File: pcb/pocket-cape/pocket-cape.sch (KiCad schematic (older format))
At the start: 28 parts, among them J1 PhDiode1, J2 12V, J3 PhDiode2, U1 MIC920, U2 74LVC2G14GV, U3 ULN2003A, U4 AP3211, U5 MIC920

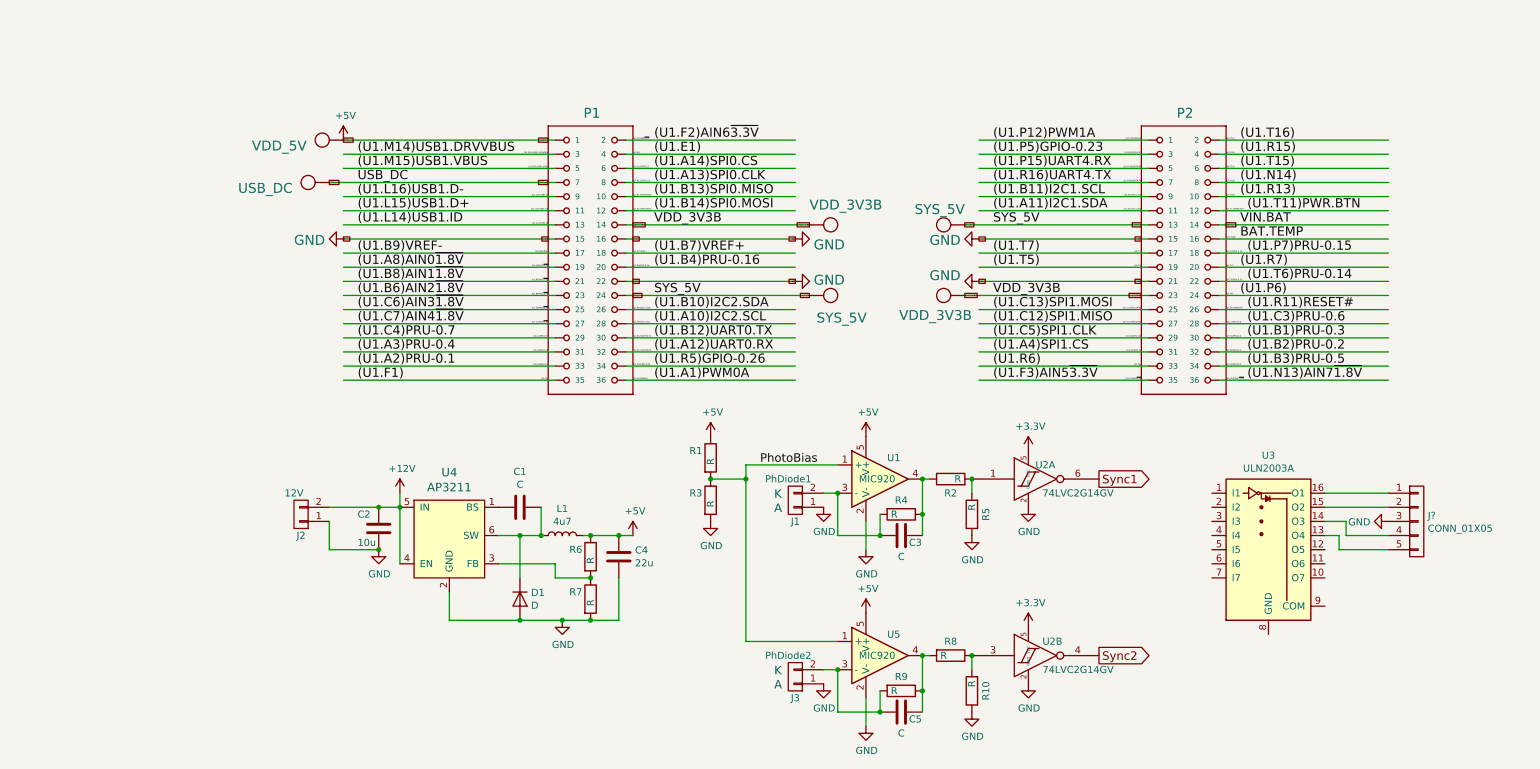
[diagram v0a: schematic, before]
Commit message: Pocket Cape, pre-routing.
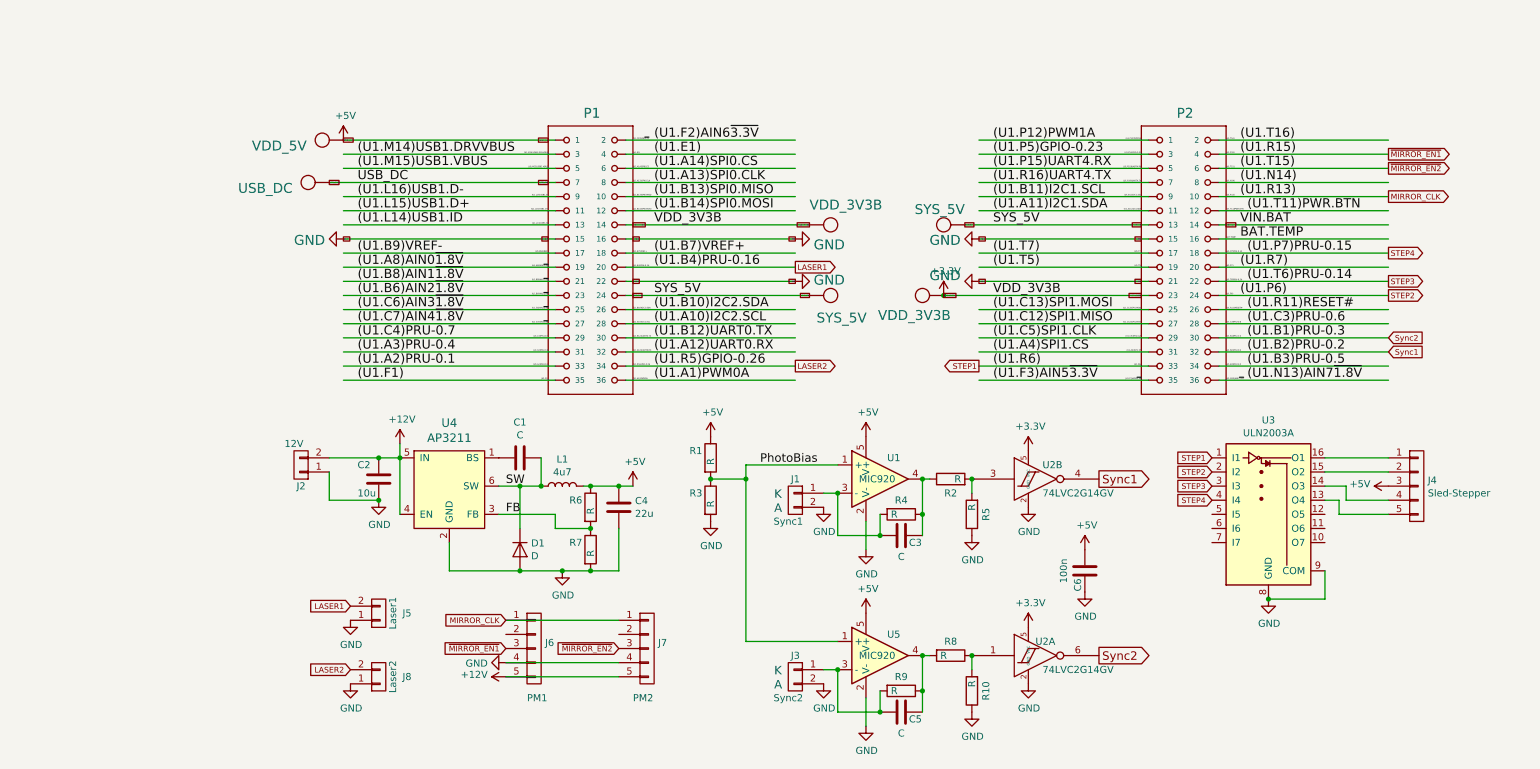
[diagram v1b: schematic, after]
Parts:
- added C6: 100n, Capacitors_SMD:C_0603, symbol C
- added J5: Laser1, Pin_Headers:Pin_Header_Straight_1x02_Pitch2.54mm, symbol CONN_01X02
- added J6: PM1, Pin_Headers:Pin_Header_Straight_1x05_Pitch2.54mm, symbol CONN_01X05
- added J7: PM2, Pin_Headers:Pin_Header_Straight_1x05_Pitch2.54mm, symbol CONN_01X05
- added J8: Laser2, Pin_Headers:Pin_Header_Straight_1x02_Pitch2.54mm, symbol CONN_01X02
- J1: value PhDiode1 -> Sync1
- J2: footprint Pin_Headers:Pin_Header_Angled_1x02_Pitch2.54mm -> Pin_Headers:Pin_Header_Straight_1x02_Pitch2.54mm
- J3: value PhDiode2 -> Sync2
- J4: renamed from J?; value CONN_01X05 -> Sled-Stepper; footprint Pin_Headers:Pin_Header_Angled_1x05_Pitch2.54mm -> Pin_Headers:Pin_Header_Straight_1x05_Pitch2.54mm
- U3: footprint Housings_SSOP:TSSOP-16_4.4x5mm_Pitch0.65mm -> Housings_SOIC:SOIC-16_3.9x9.9mm_Pitch1.27mm
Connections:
- net labels added: FB, LASER1, LASER2, MIRROR_CLK, STEP1, STEP2, STEP3, STEP4, SW, ~MIRROR_EN1, ~MIRROR_EN2
- wire segments 114 -> 119
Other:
- moved on the sheet: C1, C2, C4, D1, J2, J4, L1, R6, R7, U2A, U2B, U3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

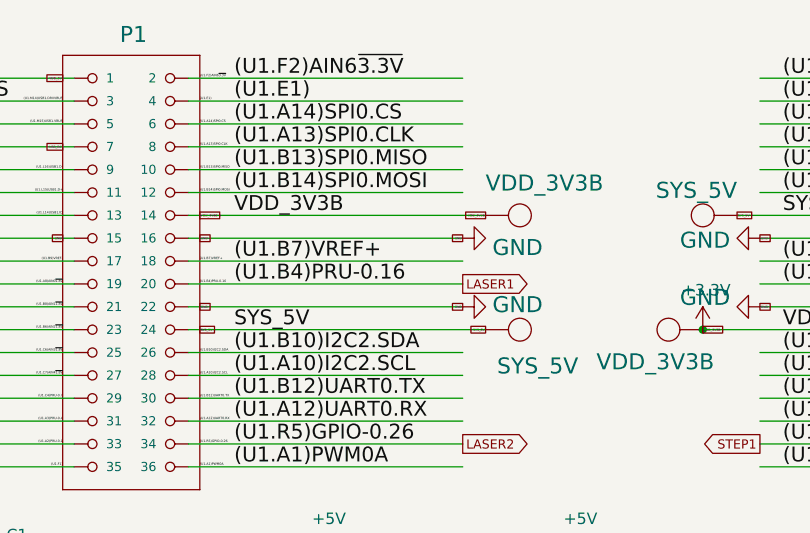
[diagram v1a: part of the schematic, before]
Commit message: First rough routing of a PocketBeagle cape.
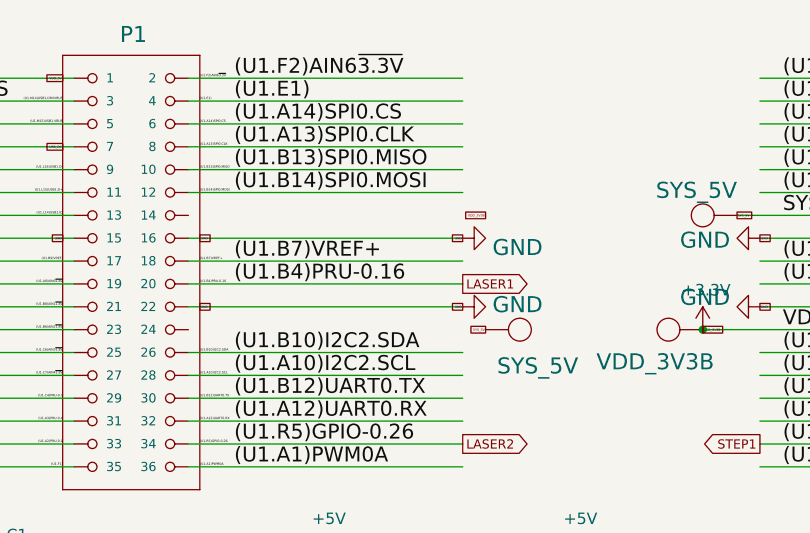
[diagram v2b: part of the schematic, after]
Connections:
- wire segments 119 -> 117
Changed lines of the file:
@@
-$EndComp
-$Comp
-L VDD_3V3B #SUPPLY011
-U 1 1 59922D07
-P 6200 3200
-F 0 "#SUPPLY011" H 6200 3360 70  0001 L BNN
-F 1 "VDD_3V3B" V 6100 3100 70  0000 L BNN
-F 2 "" H 6200 3200 60  0001 C CNN
-F 3 "" H 6200 3200 60  0001 C CNN
-	1    6200 3200
-	0    1    1    0
 $EndComp
 $Comp
@@
 SYS_5V
 Wire Wire Line
-	6100 3700 4800 3700
-Text Label 5000 3700 0    65   ~ 0
-SYS_5V
-Wire Wire Line
 	2700 2900 4300 2900
 Text Label 2900 2900 0    65   ~ 0
 USB_DC
-Wire Wire Line
-	6100 3200 4800 3200
-Text Label 5000 3200 0    65   ~ 0
-VDD_3V3B
 Wire Wire Line
 	7050 3700 8500 3700
@@
 Text GLabel 6100 3700 0    10   UnSpc ~ 0
 SYS_5V
-Text GLabel 4850 3700 2    10   UnSpc ~ 0
-SYS_5V
 Text GLabel 4250 2900 0    10   UnSpc ~ 0
 USB_DC
@@
 Text GLabel 6100 3200 0    10   UnSpc ~ 0
 VDD_3V3B
-Text GLabel 4850 3200 2    10   UnSpc ~ 0
-VDD_3V3B
 Text GLabel 7050 3700 2    10   UnSpc ~ 0

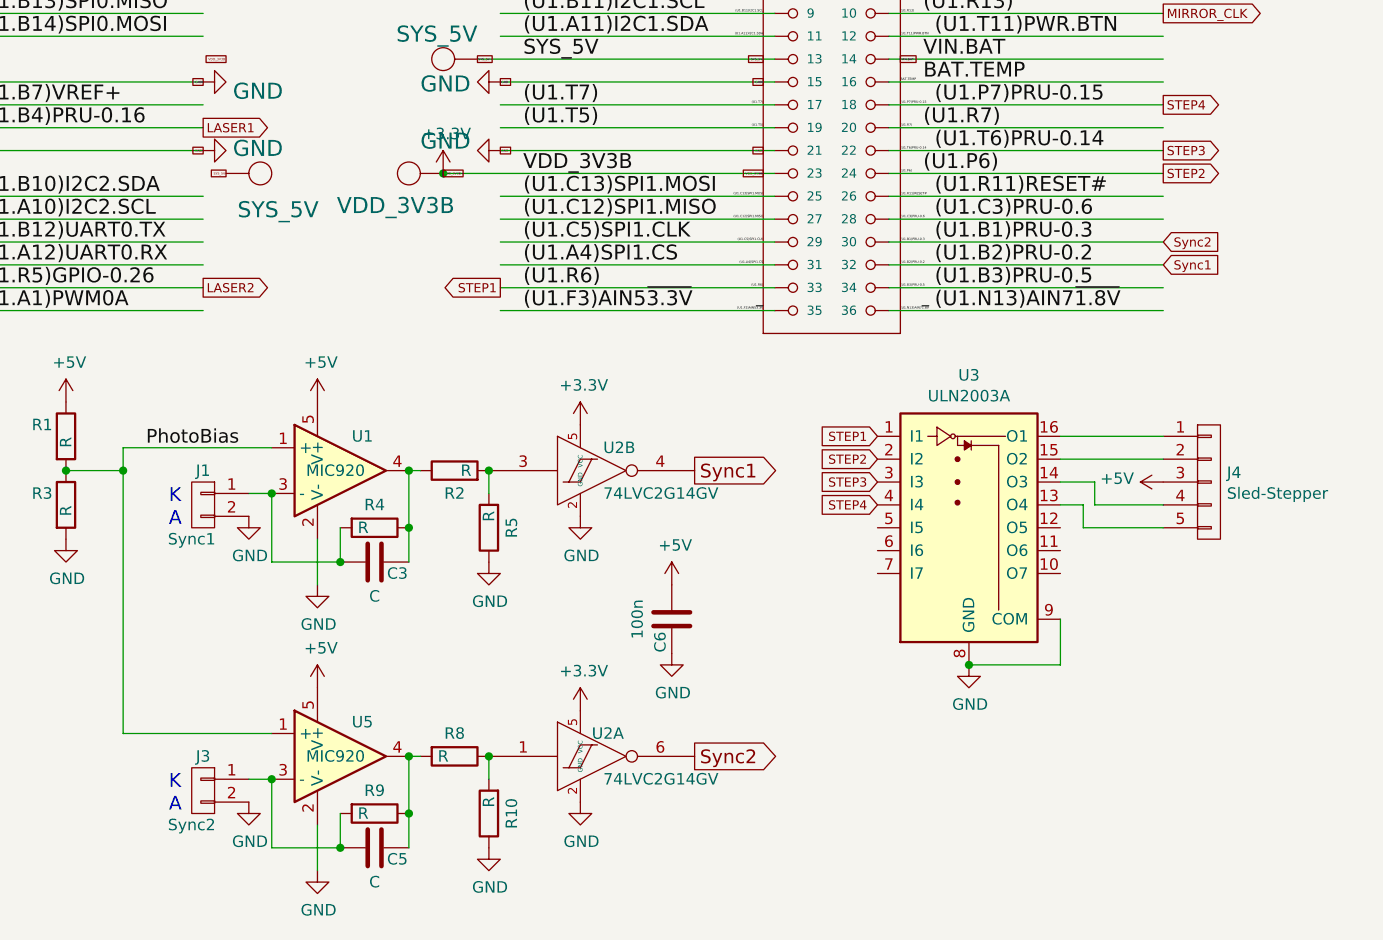
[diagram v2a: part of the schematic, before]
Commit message: Adjust header distance to accomodate space to use JST XH headers.
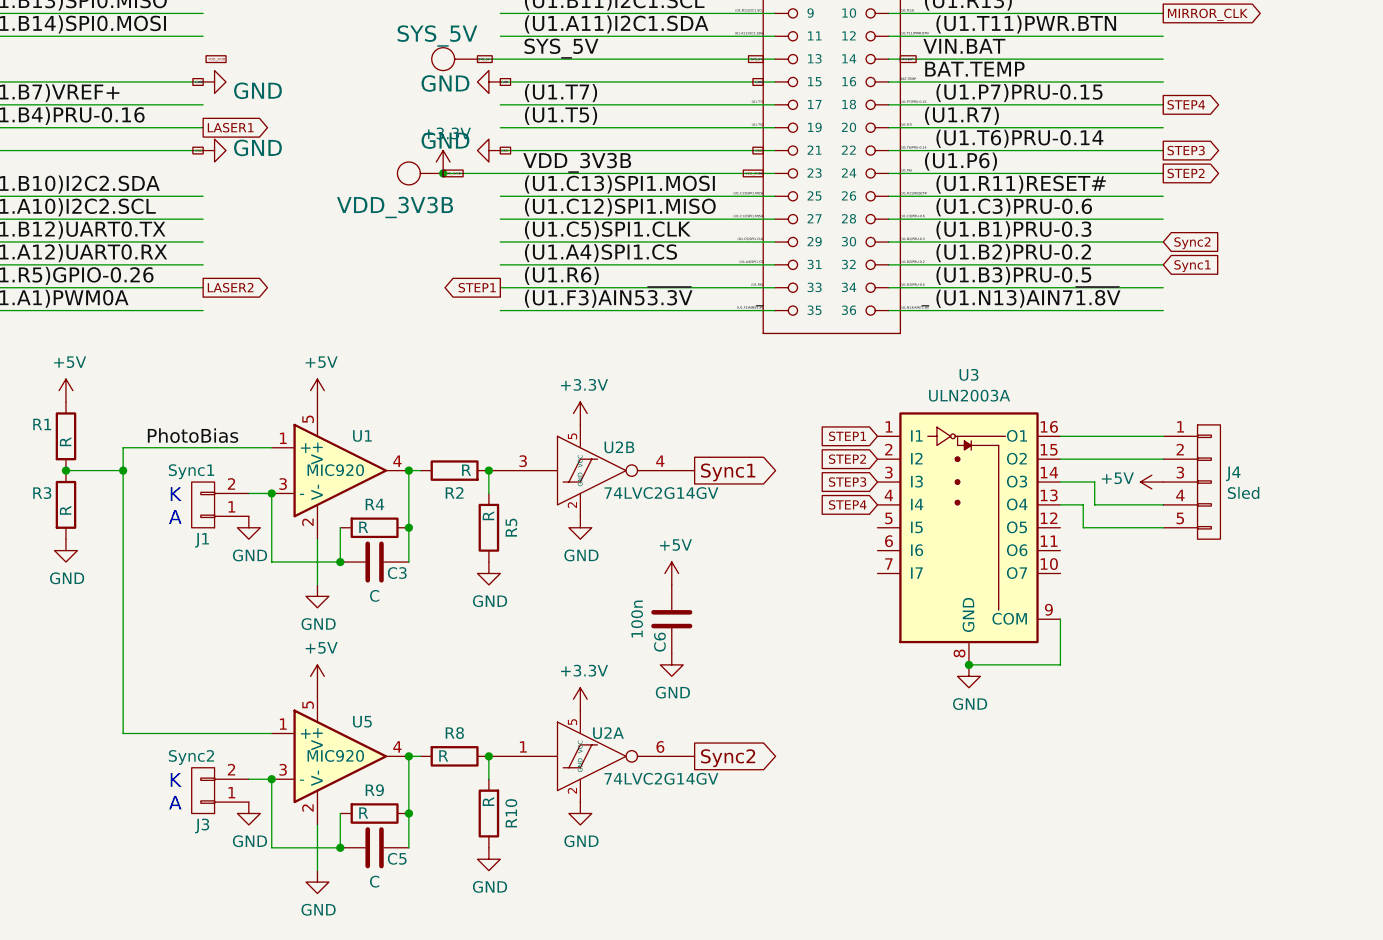
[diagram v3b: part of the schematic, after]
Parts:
- J1, J3: footprint Pin_Headers:Pin_Header_Angled_1x02_Pitch2.00mm -> Connectors_JST:JST_PH_S2B-PH-K_02x2.00mm_Angled
- J2, J5, J8: footprint Pin_Headers:Pin_Header_Straight_1x02_Pitch2.54mm -> Connectors_JST:JST_XH_B02B-XH-A_02x2.50mm_Straight
- J4: value Sled-Stepper -> Sled; footprint Pin_Headers:Pin_Header_Straight_1x05_Pitch2.54mm -> Connectors_JST:JST_XH_B05B-XH-A_05x2.50mm_Straight
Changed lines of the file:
@@
 LIBS:ldgraphy
 LIBS:pocket-cape-cache
-LIBS:ldgraphy-cape-cache
 EELAYER 26 0
 EELAYER END
@@
 	1    7100 3200
 	0    -1   -1   0
-$EndComp
-$Comp
-L SYS_5V #SUPPLY06
-U 1 1 59922B77
-P 6200 3700
-F 0 "#SUPPLY06" H 6200 3860 70  0001 L BNN
-F 1 "SYS_5V" V 6400 3650 70  0000 L BNN
-F 2 "" H 6200 3700 60  0001 C CNN
-F 3 "" H 6200 3700 60  0001 C CNN
-	1    6200 3700
-	0    1    1    0
 $EndComp
 $Comp
@@
 Text GLabel 8450 3200 0    10   UnSpc ~ 0
 SYS_5V
-Text GLabel 6100 3700 0    10   UnSpc ~ 0
-SYS_5V
 Text GLabel 4250 2900 0    10   UnSpc ~ 0
 USB_DC
@@
 F 0 "J1" H 6000 5300 50  0000 C CNN
 F 1 "Sync1" H 6050 5000 50  0000 C CNN
-F 2 "Pin_Headers:Pin_Header_Angled_1x02_Pitch2.00mm" H 6000 5150 50  0001 C CNN
+F 2 "Connectors_JST:JST_PH_S2B-PH-K_02x2.00mm_Angled" H 6000 5150 50  0001 C CNN
 F 3 "" H 6000 5150 50  0001 C CNN
 	1    6000 5150
-	-1   0    0    -1
+	-1   0    0    1
 $EndComp
 $Comp
@@
 F 0 "J3" H 6000 6550 50  0000 C CNN
 F 1 "Sync2" H 6050 6250 50  0000 C CNN
-F 2 "Pin_Headers:Pin_Header_Angled_1x02_Pitch2.00mm" H 6000 6400 50  0001 C CNN
+F 2 "Connectors_JST:JST_PH_S2B-PH-K_02x2.00mm_Angled" H 6000 6400 50  0001 C CNN
 F 3 "" H 6000 6400 50  0001 C CNN
 	1    6000 6400
-	-1   0    0    -1
+	-1   0    0    1
 $EndComp
 $Comp
@@
 F 0 "J2" H 2500 5050 50  0000 C CNN
 F 1 "12V" H 2550 4750 50  0000 C CNN
-F 2 "Pin_Headers:Pin_Header_Straight_1x02_Pitch2.54mm" H 2500 4900 50  0001 C CNN
+F 2 "Connectors_JST:JST_XH_B02B-XH-A_02x2.50mm_Straight" H 2500 4900 50  0001 C CNN
 F 3 "" H 2500 4900 50  0001 C CNN
 	1    2500 4900
@@
 P 10400 5050
 F 0 "J4" H 10478 5091 50  0000 L CNN
-F 1 "Sled-Stepper" H 10478 5000 50  0000 L CNN
-F 2 "Pin_Headers:Pin_Header_Straight_1x05_Pitch2.54mm" H 10400 5050 50  0001 C CNN
+F 1 "Sled" H 10478 5000 50  0000 L CNN
+F 2 "Connectors_JST:JST_XH_B05B-XH-A_05x2.50mm_Straight" H 10400 5050 50  0001 C CNN
 F 3 "" H 10400 5050 50  0001 C CNN
 	1    10400 5050
@@
 F 0 "J5" H 3250 5950 50  0000 C CNN
 F 1 "Laser1" V 3150 5950 50  0000 C CNN
-F 2 "Pin_Headers:Pin_Header_Straight_1x02_Pitch2.54mm" H 3050 5950 50  0001 C CNN
+F 2 "Connectors_JST:JST_XH_B02B-XH-A_02x2.50mm_Straight" H 3050 5950 50  0001 C CNN
 F 3 "" H 3050 5950 50  0001 C CNN
 	1    3050 5950
@@
 F 0 "J8" H 3250 6400 50  0000 C CNN
 F 1 "Laser2" V 3150 6400 50  0000 C CNN
-F 2 "Pin_Headers:Pin_Header_Straight_1x02_Pitch2.54mm" H 3050 6400 50  0001 C CNN
+F 2 "Connectors_JST:JST_XH_B02B-XH-A_02x2.50mm_Straight" H 3050 6400 50  0001 C CNN
 F 3 "" H 3050 6400 50  0001 C CNN
 	1    3050 6400

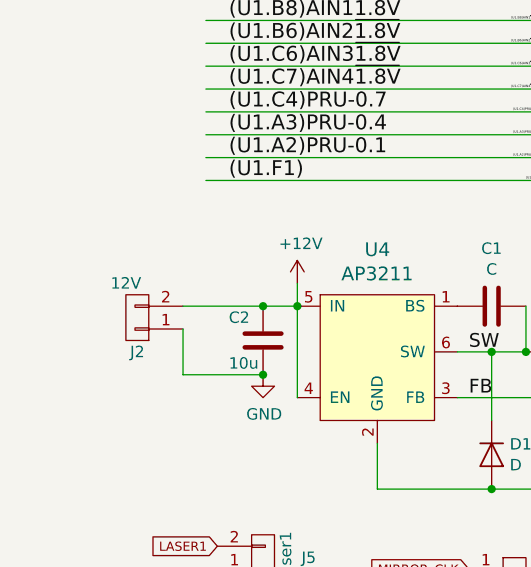
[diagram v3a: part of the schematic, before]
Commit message: Move component labels for better readability.
Also add signal labels on the PocketBeagle header for easier testpoint
finding.
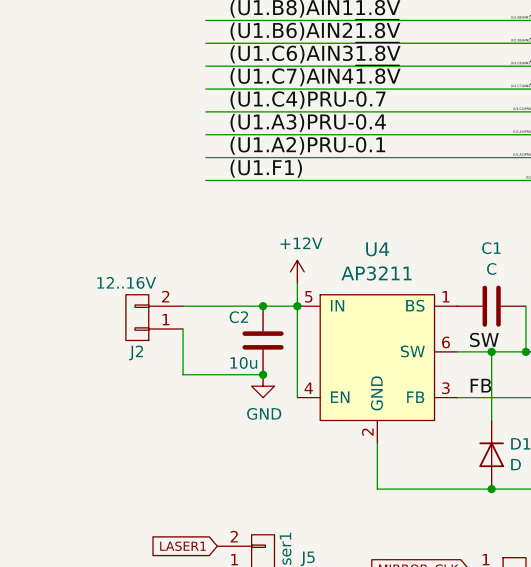
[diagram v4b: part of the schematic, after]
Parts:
- J2: value 12V -> 12..16V
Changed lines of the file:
@@
 P 2500 4900
 F 0 "J2" H 2500 5050 50  0000 C CNN
-F 1 "12V" H 2550 4750 50  0000 C CNN
+F 1 "12..16V" H 2550 4750 50  0000 C CNN
 F 2 "Connectors_JST:JST_XH_B02B-XH-A_02x2.50mm_Straight" H 2500 4900 50  0001 C CNN
 F 3 "" H 2500 4900 50  0001 C CNN

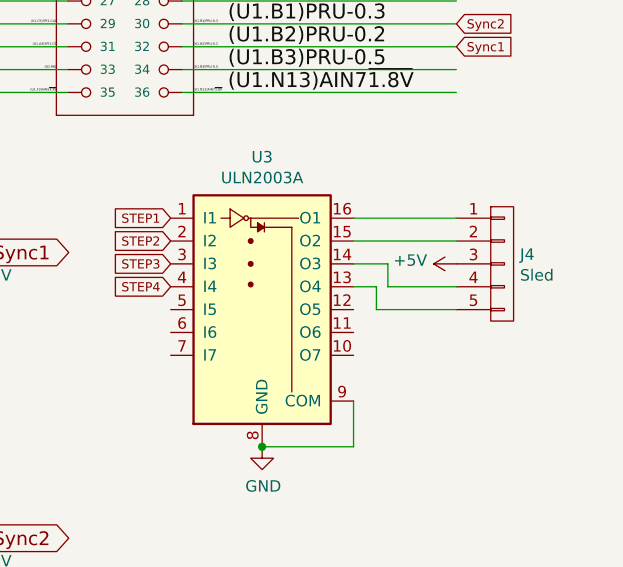
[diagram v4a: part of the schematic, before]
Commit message: Fix wrong connection to stepper connector.
o common is not the center tap, but Pin5
o Also some more labelling (e.g. adding RX/TX)
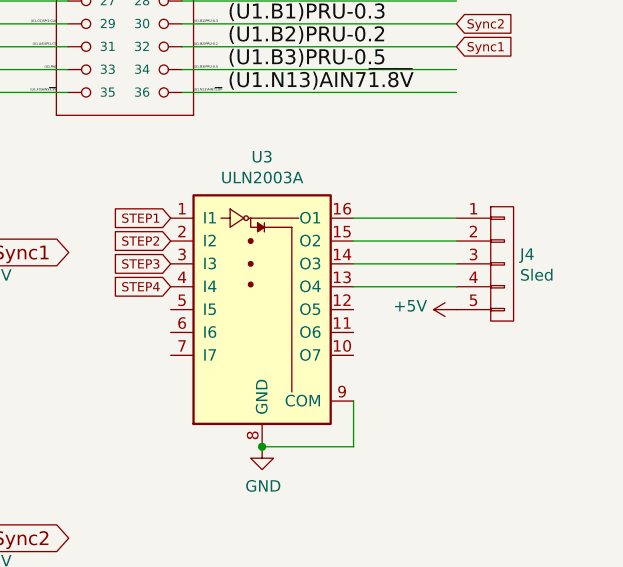
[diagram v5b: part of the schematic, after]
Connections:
- wire segments 117 -> 113
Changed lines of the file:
@@
 	1    0    0    -1
 $EndComp
-Wire Wire Line
-	9750 5150 9850 5150
-Wire Wire Line
-	9850 5150 9850 5250
-Wire Wire Line
-	9850 5250 10200 5250
-Wire Wire Line
-	9750 5050 9900 5050
-Wire Wire Line
-	9900 5050 9900 5150
-Wire Wire Line
-	9900 5150 10200 5150
 $Comp
 L CONN_01X05 J7
@@
 L +5V #PWR020
 U 1 1 59CF0516
-P 10200 5050
-F 0 "#PWR020" H 10200 4900 50  0001 C CNN
-F 1 "+5V" V 10215 5178 50  0000 L CNN
-F 2 "" H 10200 5050 50  0001 C CNN
-F 3 "" H 10200 5050 50  0001 C CNN
-	1    10200 5050
+P 10200 5250
+F 0 "#PWR020" H 10200 5100 50  0001 C CNN
+F 1 "+5V" V 10215 5378 50  0000 L CNN
+F 2 "" H 10200 5250 50  0001 C CNN
+F 3 "" H 10200 5250 50  0001 C CNN
+	1    10200 5250
 	0    -1   -1   0
 $EndComp
@@
 Text GLabel 10200 4100 2    40   Input ~ 0
 Sync1
+Wire Wire Line
+	9750 5050 10200 5050
+Wire Wire Line
+	9750 5150 10200 5150
 $EndSCHEMATC

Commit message: Use three-way connector for Laser (GND - signal - 12V)
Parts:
- J5, J8: footprint Connectors_JST:JST_XH_B02B-XH-A_02x2.50mm_Straight -> Connectors_JST:JST_XH_B03B-XH-A_03x2.50mm_Straight; symbol CONN_01X02 -> CONN_01X03
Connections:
- net labels added: STEP_A1, STEP_A2, STEP_B1, STEP_B2
- net labels removed: STEP1, STEP2, STEP3, STEP4
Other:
- moved on the sheet: C1, C2, C3, C4, C5, C6, D1, J1, J2, J3, J4, J6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
